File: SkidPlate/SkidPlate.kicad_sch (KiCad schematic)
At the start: 10 parts, among them U2 BNO055, U3 IC_PMW3360DM-T2QU

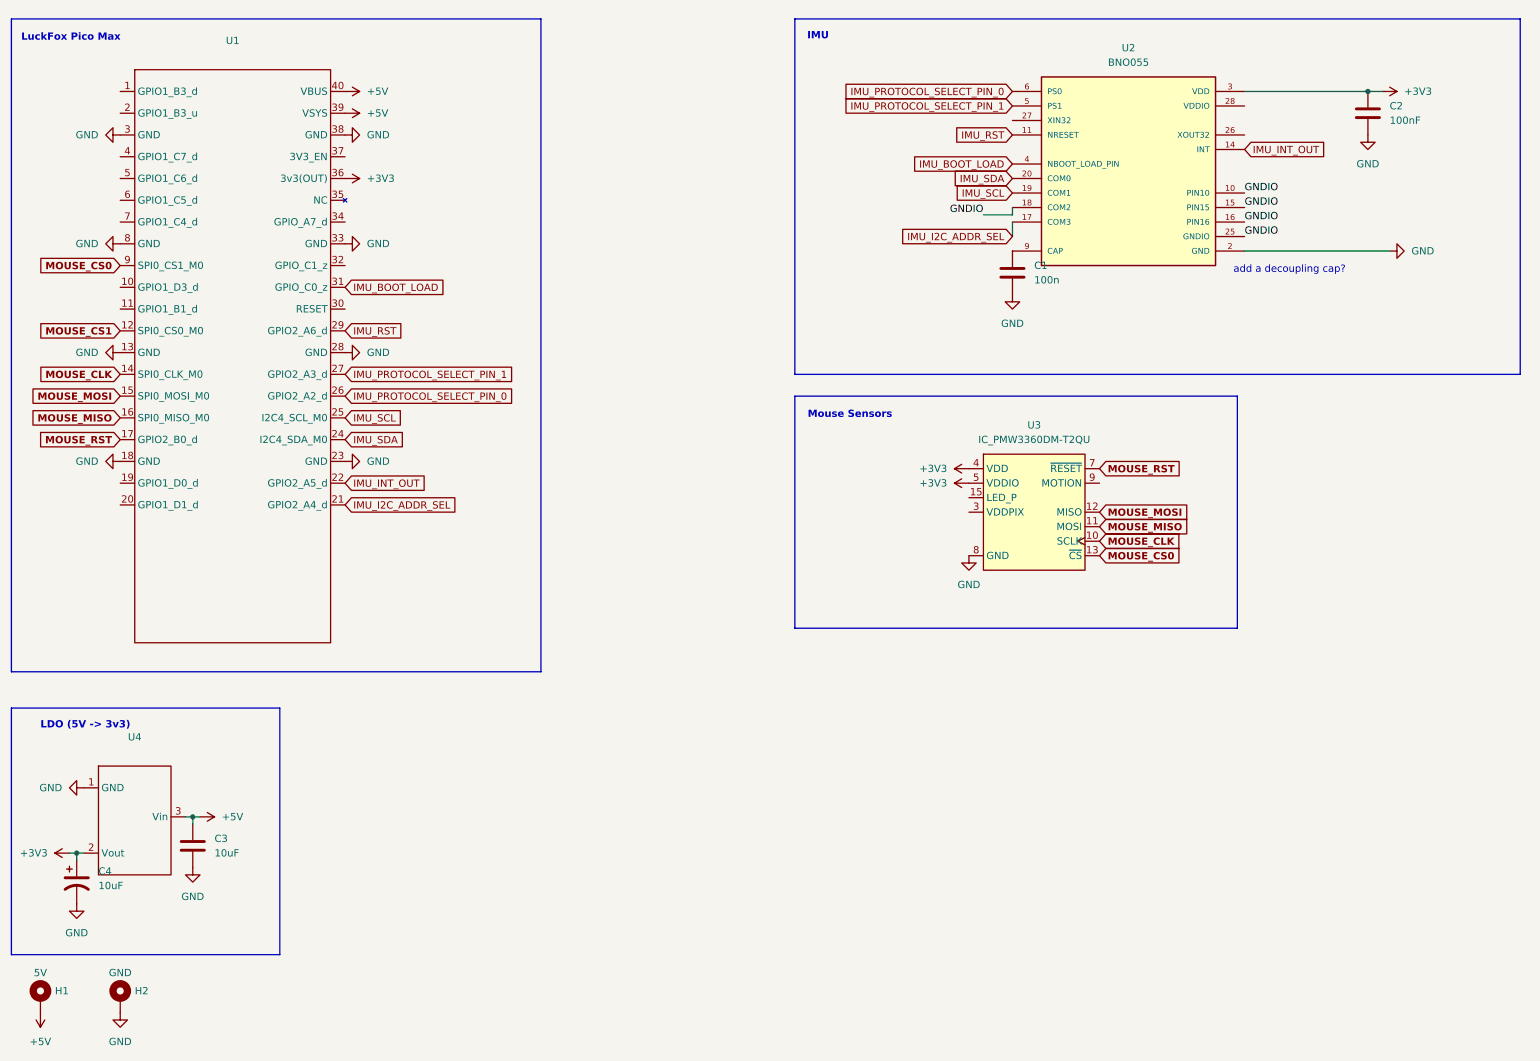
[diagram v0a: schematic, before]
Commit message: update skidplate schematic with new imu
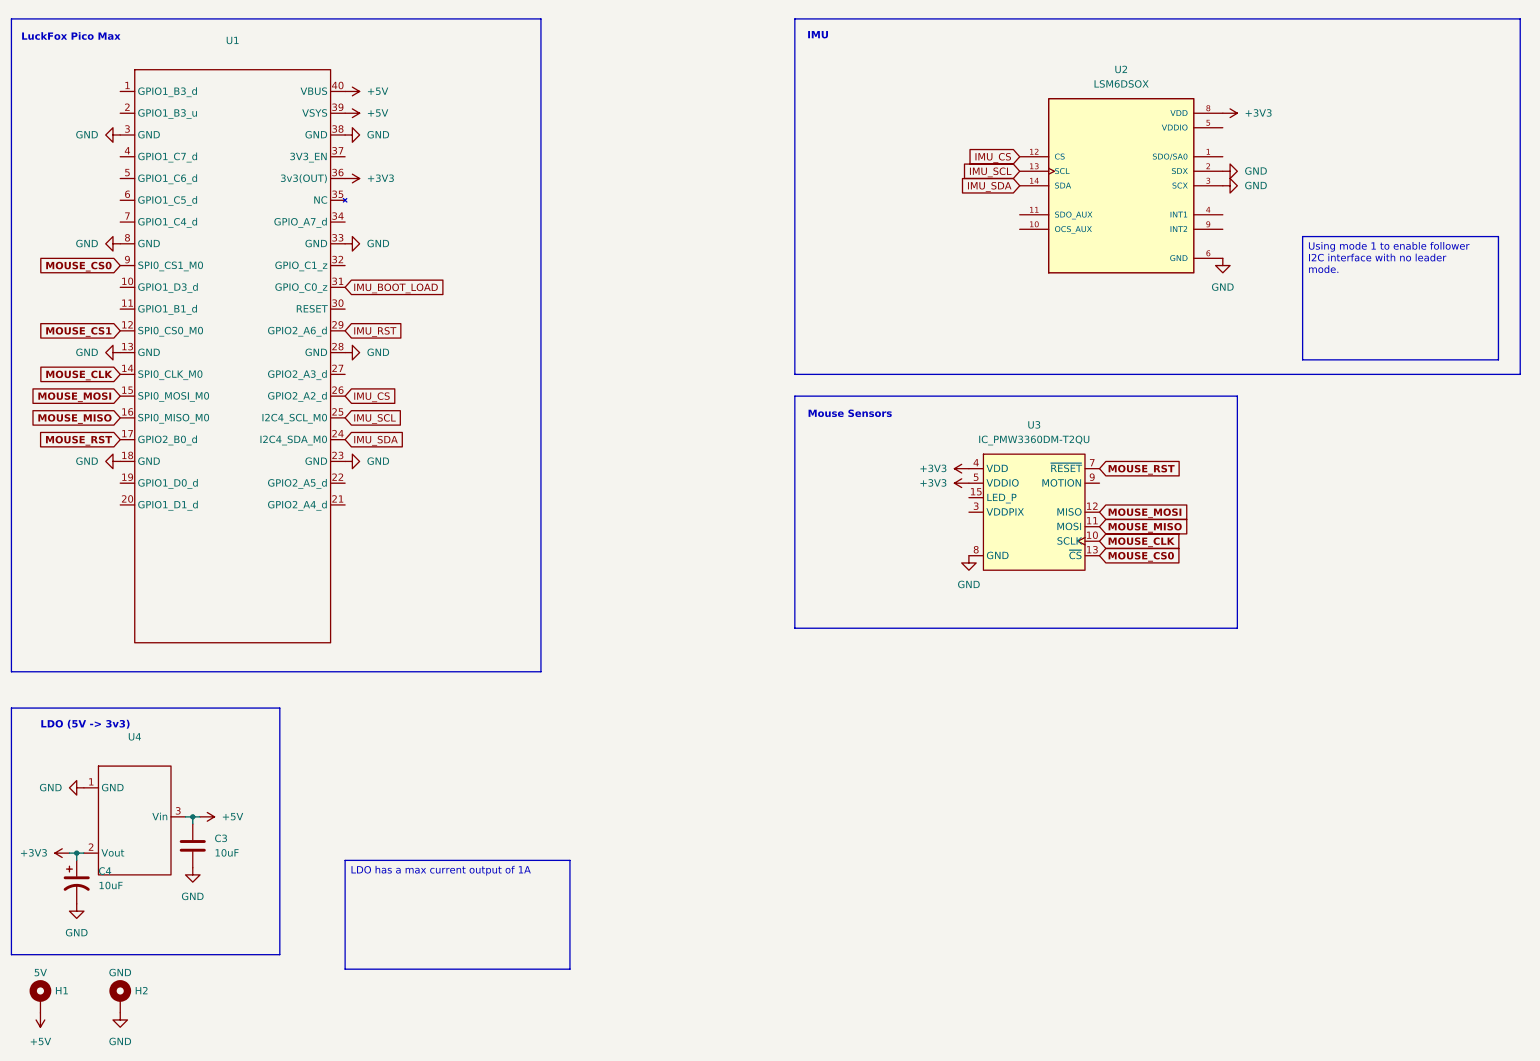
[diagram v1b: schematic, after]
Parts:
- removed C1: 100n, bots:C_0603_1608Metric, symbol bots:C_0.1u
- removed C2: 100nF, Capacitor_SMD:C_1206_3216Metric, symbol Device:C
- removed U2: BNO055, bots:LGA28R50P4X10_380X520X100, symbol bots:BNO055
- added U2: LSM6DSOX, bots:PQFN50P300X250X86-14N, symbol bots:LSM6DSOX
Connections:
- net +3V3: now also U2.8 (VDD)
- net GND: now also U2.2 (SDX), U2.3 (SCX), U2.6 (GND), U2.7 (GND)
- net IMU_SCL: now also U2.13 (SCL)
- net IMU_SDA: now also U2.14 (SDA)
- net IMU_I2C_ADDR_SEL: no longer names the net of U1.21 (GPIO2_A4_d)
- net IMU_INT_OUT: no longer names the net of U1.22 (GPIO2_A5_d)
- net IMU_PROTOCOL_SELECT_PIN_0 renamed IMU_CS
- net IMU_CS: now also U2.12 (CS)
- net IMU_PROTOCOL_SELECT_PIN_1: no longer names the net of U1.27 (GPIO2_A3_d)
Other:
- note removed: "add a decoupling cap?"

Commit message: updated skidplate schematic, need to add usb pd
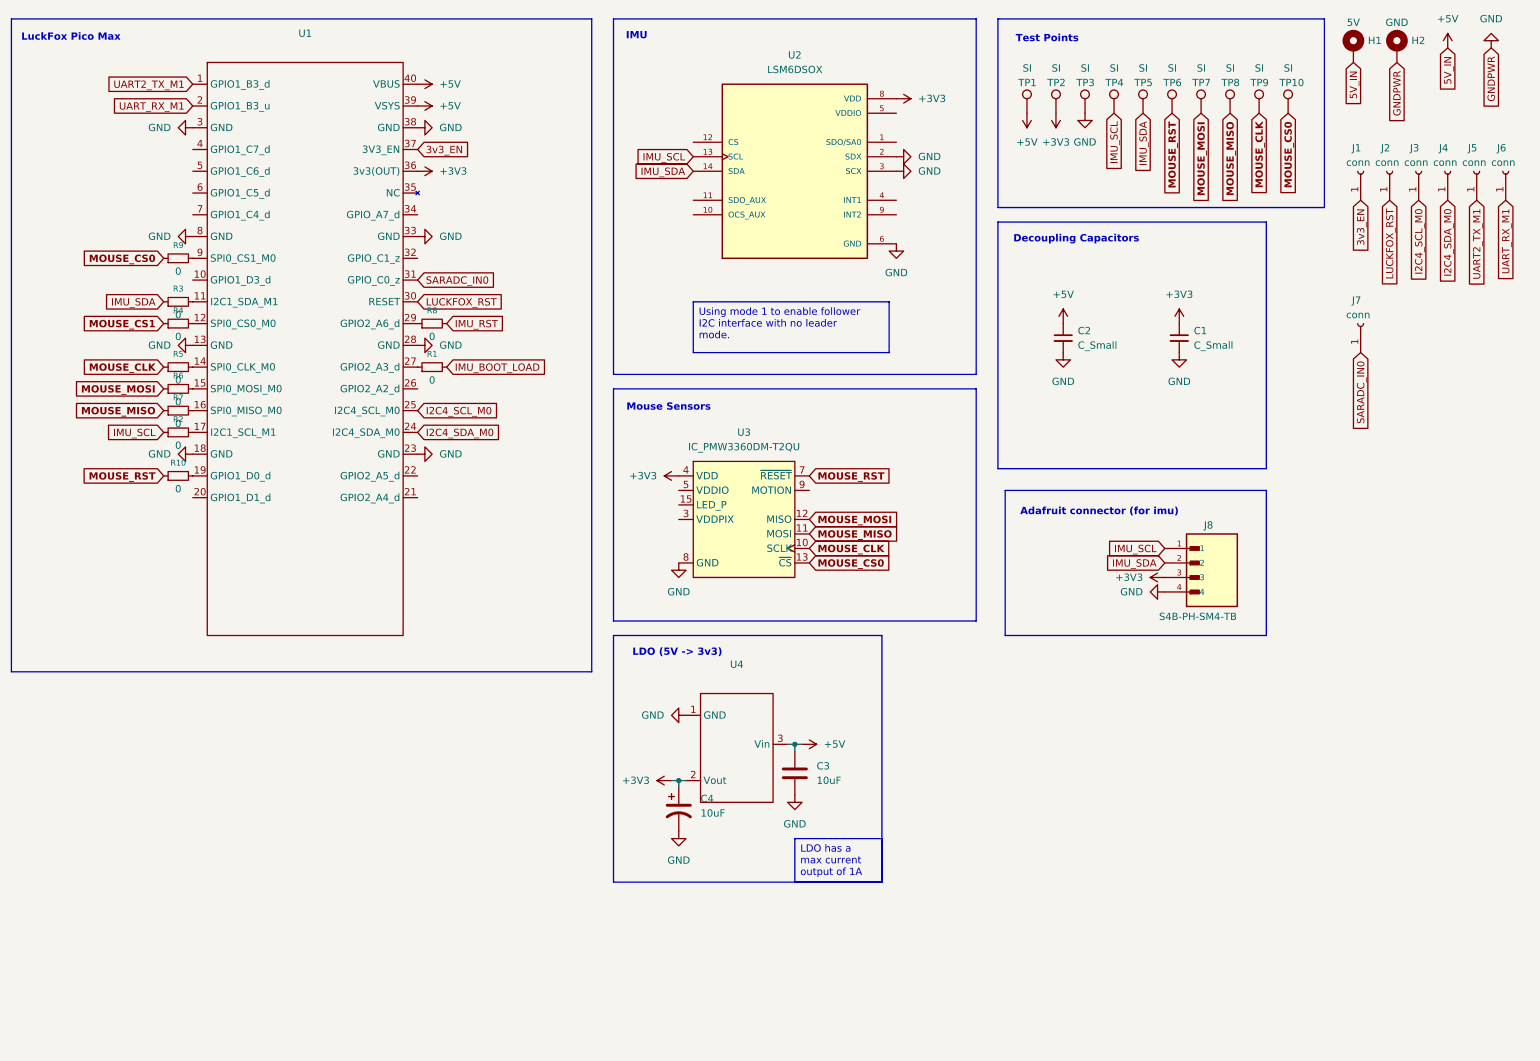
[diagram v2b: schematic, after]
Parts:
- added C1, C2: C_Small, bots:C_0603_1608Metric, symbol Device:C_Small
- added J1, J2, J3, J4, J5, J6, J7: conn, symbol Connector:Conn_01x01_Socket
- added J8: S4B-PH-SM4-TB, S4B-PH-SM4-TB:JST_S4B-PH-SM4-TB, symbol bots:S4B-PH-SM4-TB
- added R1, R10, R2, R3, R4, R5, R6, R7, R8, R9: 0, bots:R_0603_1608Metric, symbol Device:R_Small
- added TP1, TP10, TP2, TP3, TP4, TP5, TP6, TP7, TP8, TP9: SI, bots:pad_0603, symbol bots:TestPoint_1x1
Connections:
- net +3V3: now also C1.1, J8.3, TP2.1; no longer U3.5 (VDDIO)
- net +5V: now also C2.1, TP1.1
- net GND: now also C1.2, C2.2, J8.4, TP3.1
- net IMU_BOOT_LOAD: now also R1.2; no longer U1.31 (GPIO_C0_z)
- net IMU_RST: now also R8.2; no longer U1.29 (GPIO2_A6_d)
- net IMU_SCL: now also J8.1, R2.1, TP4.1; no longer U1.25 (I2C4_SCL_M0)
- net IMU_SDA: now also J8.2, R3.1, TP5.1; no longer U1.24 (I2C4_SDA_M0)
- net MOUSE_CLK: now also R5.1, TP9.1; no longer U1.14 (SPI0_CLK_M0)
- net MOUSE_CS0: now also R9.1, TP10.1; no longer U1.9 (SPI0_CS1_M0)
- net MOUSE_CS1: now also R4.1; no longer U1.12 (SPI0_CS0_M0)
- net MOUSE_MISO: now also R7.1, TP8.1; no longer U1.16 (SPI0_MISO_M0)
- net MOUSE_MOSI: now also R6.1, TP7.1; no longer U1.15 (SPI0_MOSI_M0)
- net MOUSE_RST: now also R10.1, TP6.1; no longer U1.17 (GPIO2_B0_d)
- net UART2_TX_M1: now reaches U1.1 (GPIO1_B3_d)
- net UART2_TX_M1: now also J5.1 (Pin_1)
- net at U1.11 (I2C1_SDA_M1): now also R3.2
- net at U1.19 (GPIO1_D0_d): now also R10.2
- net UART_RX_M1: now reaches U1.2 (GPIO1_B3_u)
- net UART_RX_M1: now also J6.1 (Pin_1)
- net at U1.27 (GPIO2_A3_d): now also R1.1
- net LUCKFOX_RST: now reaches U1.30 (RESET)
- net LUCKFOX_RST: now also J2.1 (Pin_1)
- net 3v3_EN: now reaches U1.37 (3V3_EN)
- net 3v3_EN: now also J1.1 (Pin_1)
- net IMU_CS: no longer names the net of U2.12 (CS)
- net IMU_CS: no longer U1.26 (GPIO2_A2_d)
- new net: R2.2, U1.17 (I2C1_SCL_M1)
- new net: R8.1, U1.29 (GPIO2_A6_d)
- new net: R5.2, U1.14 (SPI0_CLK_M0)
- new net: R4.2, U1.12 (SPI0_CS0_M0)
- new net: R9.2, U1.9 (SPI0_CS1_M0)
- new net: R7.2, U1.16 (SPI0_MISO_M0)
- new net: R6.2, U1.15 (SPI0_MOSI_M0)
- new net I2C4_SCL_M0: J3.1 (Pin_1), U1.25 (I2C4_SCL_M0)
- new net I2C4_SDA_M0: J4.1 (Pin_1), U1.24 (I2C4_SDA_M0)
- new net SARADC_IN0: J7.1 (Pin_1), U1.31 (GPIO_C0_z)
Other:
- note added: "Adafruit connector (for imu)"
- note added: "Decoupling Capacitors"
- note added: "Test Points"
- moved on the sheet: C3, C4, H1, H2, U1, U2, U3, U4

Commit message: midplate additions WIP
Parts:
- removed C1, C2: C_Small, bots:C_0603_1608Metric, symbol Device:C_Small
- removed C3: 10uF, Capacitor_SMD:C_1206_3216Metric, symbol Device:C
- removed C4: 10uF, bots:CAP_25SVPF100M, symbol bots:C_1000u_POL
- removed J1, J2, J3, J4, J5, J6, J7: conn, symbol Connector:Conn_01x01_Socket
- removed R1, R10, R2, R3, R4, R5, R6, R7, R8, R9: 0, bots:R_0603_1608Metric, symbol Device:R_Small
- removed TP10, TP6, TP7, TP8, TP9: SI, bots:pad_0603, symbol bots:TestPoint_1x1
- removed U1: ~, bots:RV1106_PICO_MAX, symbol bots:RV1106_PICO_MAX
- removed U3: IC_PMW3360DM-T2QU, bots:IC_PMW3360DM-T2QU 16Pin, symbol bots:IC_PMW3360DM-T2QU
- removed U4: ~, Package_TO_SOT_SMD:SOT-223, symbol bots:BL1117-33-A-SOT-223
- added C3: 10u, bots:C_0805_2012Metric, symbol bots:C_10u
- added C4: 22u, bots:C_0603_1608Metric, symbol bots:C_22u
- added H10: RPI1, bots:MountingHole_2.7mm_M2.5_DIN965_Pad, symbol bots:MountingHoleM2.5NoThread_wConn
- added H11: RPI2, bots:MountingHole_2.7mm_M2.5_DIN965_Pad, symbol bots:MountingHoleM2.5NoThread_wConn
- added H12: RPI3, bots:MountingHole_2.7mm_M2.5_DIN965_Pad, symbol bots:MountingHoleM2.5NoThread_wConn
- added H3: CANL, bots:MountingHole_2.7mm_M2.5_DIN965_Pad, symbol bots:MountingHoleM2.5NoThread_wConn
- added H4: CANH, bots:MountingHole_2.7mm_M2.5_DIN965_Pad, symbol bots:MountingHoleM2.5NoThread_wConn
- added H5: 5V, bots:MountingHole_2.7mm_M2.5_DIN965_Pad, symbol bots:MountingHoleM2.5NoThread_wConn
- added H6: EXTRA, bots:MountingHole_2.7mm_M2.5_DIN965_Pad, symbol bots:MountingHoleM2.5NoThread_wConn
- added H7: HV, bots:MountingHole_2.7mm_M2.5_DIN965_Pad, symbol bots:MountingHoleM2.5NoThread_wConn
- added H8: CHICKER, bots:MountingHole_2.7mm_M2.5_DIN965_Pad, symbol bots:MountingHoleM2.5NoThread_wConn
- added H9: BKBM, bots:MountingHole_2.7mm_M2.5_DIN965_Pad, symbol bots:MountingHoleM2.5NoThread_wConn
- added TP11: VCC, bots:TestPoint_Pad_2.0x2.0mm, symbol bots:TestPoint_2x2
- added U1: AMS1117-3.3, bots:SOT-223-3_TabPin2, symbol bots:AMS1117-3.3
- H1: value 5V -> VCC
- H2: value GND -> PGND
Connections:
- net +3V3: now also C4.1, U1.2 (OUTPUT)
- net +5V: now also C3.1, H5.1, U1.3 (INPUT); no longer H1.1
- net GND: now also C3.2, C4.2, U1.1 (GND)
- new net BKBM: H9.1
- new net CANH: H4.1
- new net CANL: H3.1
- new net CHICKER: H8.1
- new net EXTRA: H6.1
- new net HV: H7.1
- new net VCC: H1.1, TP11.1
- no-connect marks 0 -> 3
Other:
- added sheet baseplate (baseplate.kicad_sch)
- note added: "Power Pillars"
- note added: "Structural Mounts (Rpi)"
- note removed: "Decoupling Capacitors"
- note removed: "LuckFox Pico Max"
- note removed: "Mouse Sensors"
- moved on the sheet: J8, TP1, TP2, TP3, TP4, TP5
